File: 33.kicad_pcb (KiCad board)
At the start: 2 copper layers, 187.7 x 73.8 mm, 77 parts, among them U1 ProMicro

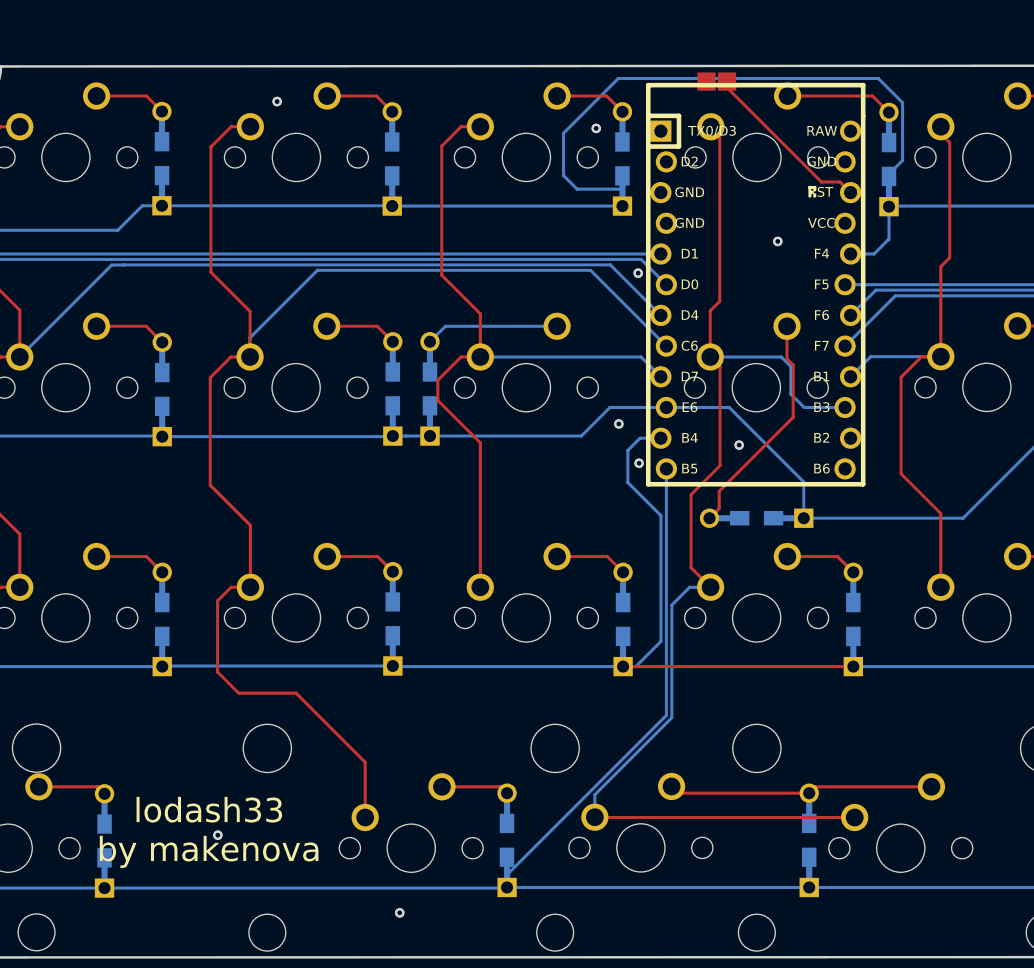
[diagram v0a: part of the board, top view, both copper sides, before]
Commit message: update reset jumper position
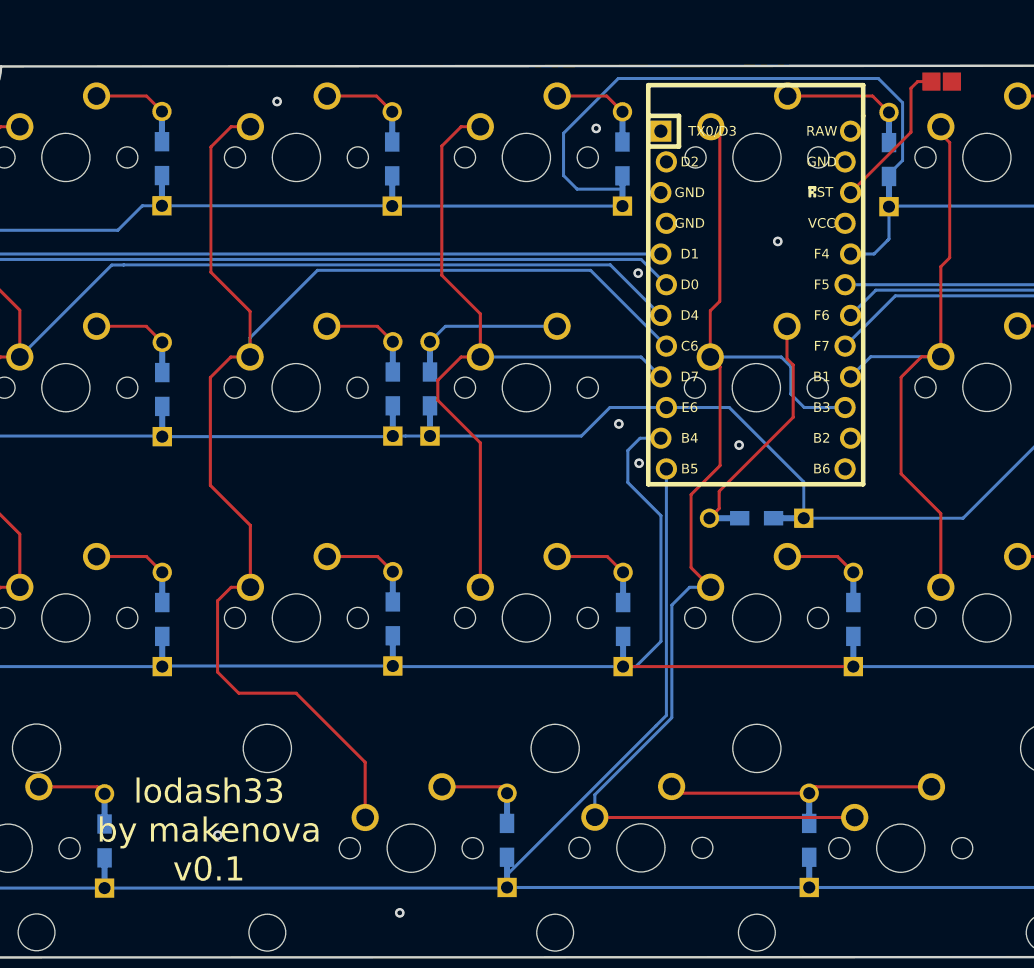
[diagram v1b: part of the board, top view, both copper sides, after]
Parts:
- moved JP1 18.6 mm to (177.5, 50.4), turned to 270 degrees
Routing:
- net RST: track 14.3 -> 12.6 mm
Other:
- board text added: "lodash33 by makenova v0.1"
- board text removed: "lodash33 by makenova"
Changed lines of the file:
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@@
   )
   (module random-keyboard-parts:Jumper-UserFriendly-Small (layer F.Cu)
-    (at 158.875 50.375 90)
+    (at 177.4825 50.375 270)
     (attr virtual)
     (fp_text reference JP1 (at 0 2.65 90) (layer Dwgs.User)
@@
       (effects (font (size 1 1) (thickness 0.15)))
     )
-    (pad 1 smd rect (at 0 -0.85 90) (size 1.5 1.5) (layers F.Cu F.Mask)
+    (pad 1 smd rect (at 0 -0.85 270) (size 1.5 1.5) (layers F.Cu F.Mask)
       (net 57 GND))
-    (pad 2 smd rect (at 0 0.85 90) (size 1.5 1.5) (layers F.Cu F.Mask)
+    (pad 2 smd rect (at 0 0.85 270) (size 1.5 1.5) (layers F.Cu F.Mask)
       (net 58 RST))
   )
@@
     (effects (font (size 3 3) (thickness 0.4)) (justify mirror))
   )
-  (gr_text "lodash33\nby makenova" (at 116.875 112.325) (layer F.SilkS)
+  (gr_text "lodash33\nby makenova\nv0.1" (at 116.875 112.325) (layer F.SilkS)
     (effects (font (size 2 2) (thickness 0.2)))
   )
@@
   (via (at 152.45 81.95) (size 0.8) (drill 0.4) (layers F.Cu B.Cu) (net 57))
   (via (at 61.475 70.275) (size 0.8) (drill 0.4) (layers F.Cu B.Cu) (net 57))
-  (segment (start 159.725 50.871002) (end 159.725 50.375) (width 0.25) (layer F.Cu) (net 58))
-  (segment (start 167.537699 58.683701) (end 159.725 50.871002) (width 0.25) (layer F.Cu) (net 58))
-  (segment (start 169.072301 58.683701) (end 167.537699 58.683701) (width 0.25) (layer F.Cu) (net 58))
-  (segment (start 169.9486 59.56) (end 169.072301 58.683701) (width 0.25) (layer F.Cu) (net 58))
+  (segment (start 169.9486 59.56) (end 174.9425 54.5661) (width 0.25) (layer F.Cu) (net 58))
+  (segment (start 174.9425 54.5661) (end 174.9425 50.927) (width 0.25) (layer F.Cu) (net 58))
+  (segment (start 175.4945 50.375) (end 176.6325 50.375) (width 0.25) (layer F.Cu) (net 58))
+  (segment (start 174.9425 50.927) (end 175.4945 50.375) (width 0.25) (layer F.Cu) (net 58))
   (zone (net 57) (net_name GND) (layer F.Cu) (hatch edge 0.508)
     (connect_pads (clearance 0.508))

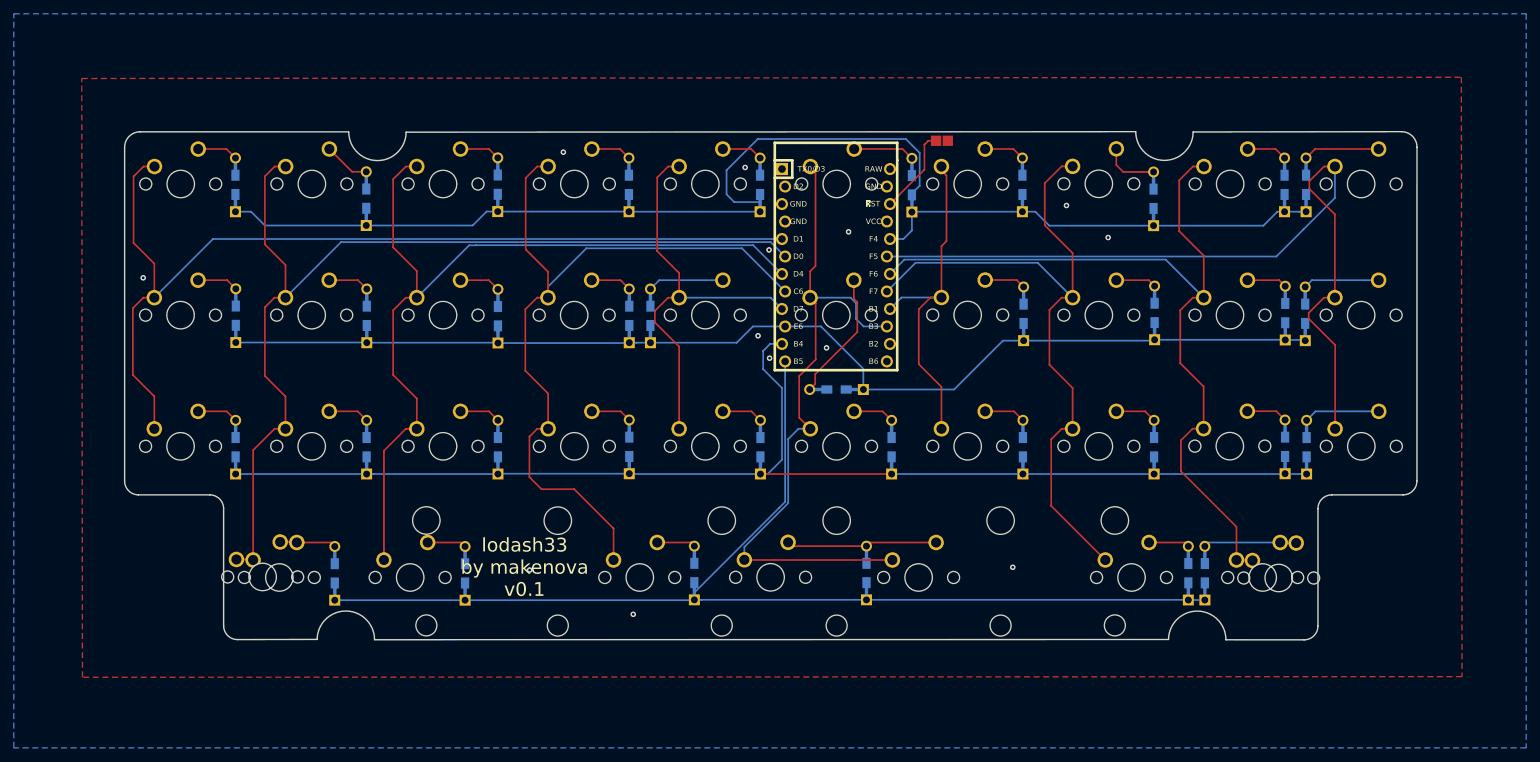
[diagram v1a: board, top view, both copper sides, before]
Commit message: breakout 4 unused pins
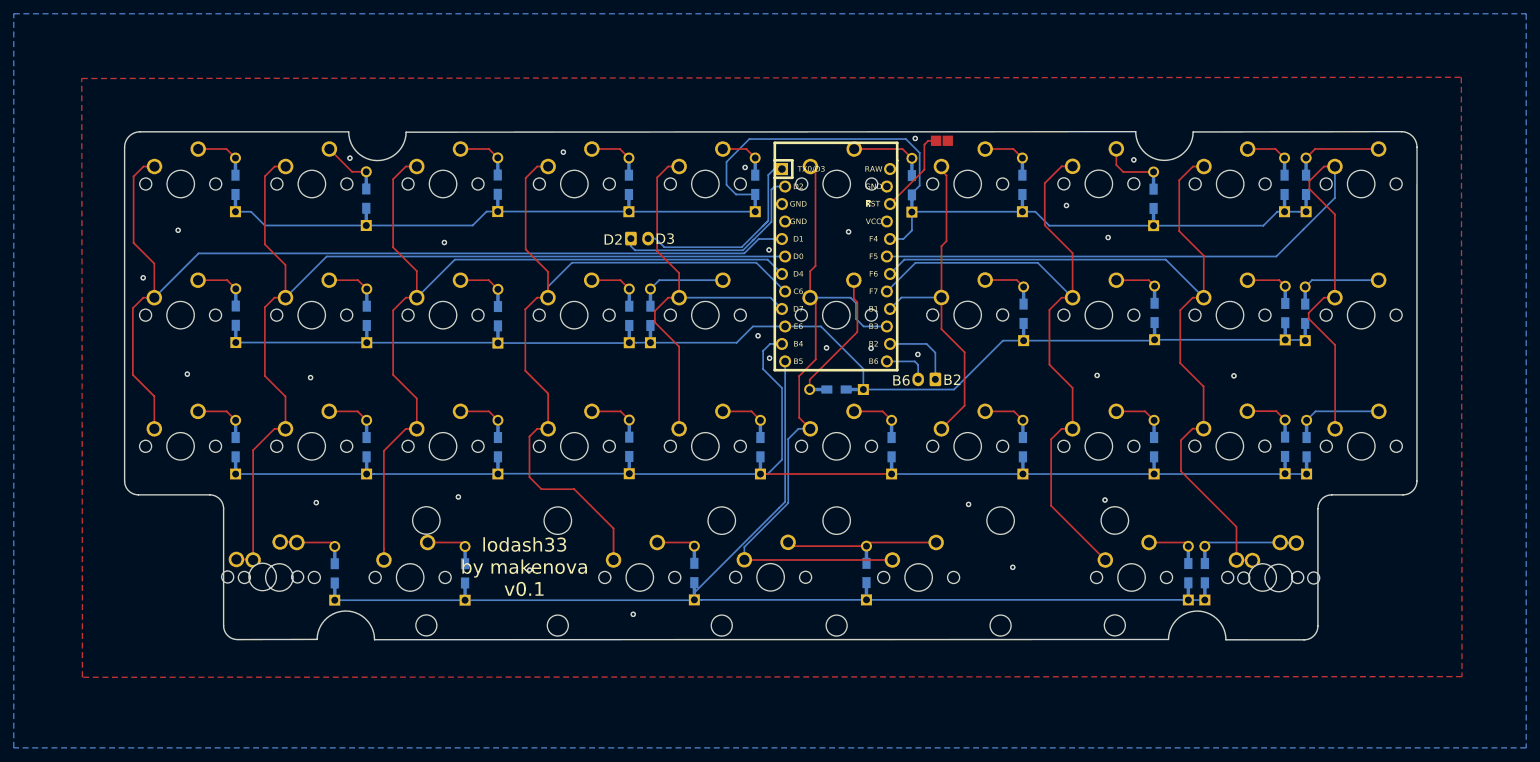
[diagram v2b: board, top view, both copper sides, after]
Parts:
- added J1: Conn_01x02_Female, Connector_JST:JST_EH_B2B-EH-A_1x02_P2.50mm_Vertical, F.Cu at (132.3, 64.6)
- added J2: Conn_01x02_Female, Connector_JST:JST_EH_B2B-EH-A_1x02_P2.50mm_Vertical, F.Cu at (176.5, 85.0)
- moved D5 0.71 mm to (150.4, 56.8)
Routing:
- net Net-(J1-Pad1): track 0.00 -> 30.6 mm
- net Net-(J1-Pad2): track 0.00 -> 29.7 mm
- net Net-(J2-Pad1): track 0.00 -> 11.0 mm
- net Net-(J2-Pad2): track 0.00 -> 6.86 mm
- net ROW0: track 189.4 -> 187.4 mm
- net COL3: track 115.3 -> 113.6 mm
- net COL2: track 125.5 -> 123.8 mm
- net COL1: track 146.1 -> 144.4 mm
- net COL6: track 50.5 -> 49.7 mm
- net Net-(D5-Pad2): track 5.95 -> 5.26 mm
- net GND: vias 13 -> 28
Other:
- board text added: "B2"
- board text added: "B6"
- board text added: "D2"
- board text added: "D3"
